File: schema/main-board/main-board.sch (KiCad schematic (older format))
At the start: 75 parts, among them P1 TST, P10 TST, P11 CONN_20, P12 CONN_4, P13 CONN_4, P14 CONN_4, P2 TST, P3 TST, P4 TST, P5 TST, P6 TST, P7 TST, P8 TST, P9 TST, Q1 bc847, Q2 si2301, Q3 si2301, Q4 irll2703, Q5 bc847, Q6 bc857, Q7 si2301, Q8 si2301, U1 L293, U2 NCP3063, U3 NCP3063

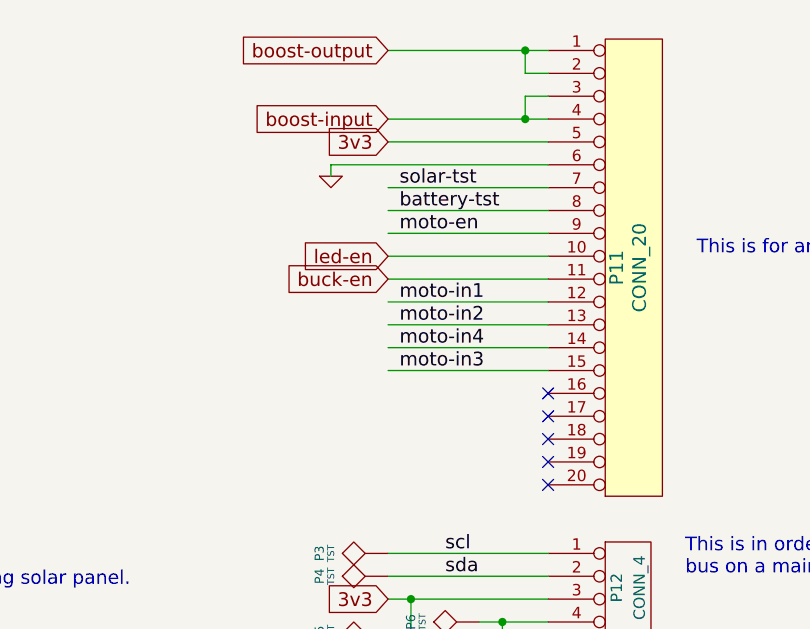
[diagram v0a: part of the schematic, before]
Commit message: Rearranged pins to match control-board's socket pinout.
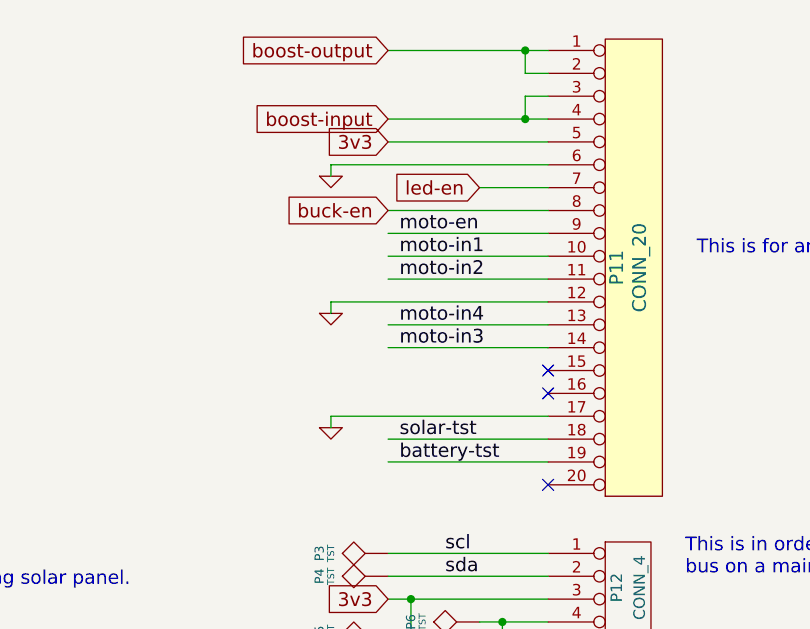
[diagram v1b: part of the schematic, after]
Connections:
- wire segments 231 -> 235
- no-connect marks 5 -> 3
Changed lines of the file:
@@
-EESchema Schematic File Version 2  date Thu 30 Aug 2012 02:28:51 PM MSK
+EESchema Schematic File Version 2  date Thu 30 Aug 2012 03:00:08 PM MSK
 LIBS:power
 LIBS:device
@@
 Comment4 ""
 $EndDescr
+NoConn ~ 4800 7450
+Wire Wire Line
+	3850 7600 3850 7550
+Wire Wire Line
+	3850 7550 4800 7550
+Wire Wire Line
+	4800 6650 4100 6650
 Connection ~ 7100 2250
 Wire Wire Line
@@
 	4800 6350 4100 6350
 Wire Wire Line
-	4800 7350 4100 7350
-Wire Wire Line
-	4800 7150 4100 7150
+	4800 7250 4100 7250
 Wire Wire Line
 	4800 6950 4100 6950
@@
 	4800 6750 4100 6750
 Wire Wire Line
-	4800 6550 4100 6550
+	4800 7650 4100 7650
 Wire Wire Line
 	7700 10300 7300 10300
@@
 Connection ~ 8950 8300
 Wire Wire Line
-	4800 6650 4100 6650
+	4800 7750 4100 7750
 Wire Wire Line
 	4800 6850 4100 6850
 Wire Wire Line
-	4800 7050 4100 7050
-Wire Wire Line
-	4800 7250 4100 7250
+	4800 7150 4100 7150
 Wire Wire Line
 	4800 6450 3850 6450
@@
 Wire Wire Line
 	6700 750  6700 2450
+Wire Wire Line
+	4800 6550 4500 6550
+Wire Wire Line
+	4800 7050 3850 7050
+Wire Wire Line
+	3850 7050 3850 7100
+$Comp
+L GND #PWR?
+U 1 1 503F475C
+P 3850 7600
+F 0 "#PWR?" H 3850 7600 30  0001 C CNN
+F 1 "GND" H 3850 7530 30  0001 C CNN
+	1    3850 7600
+	1    0    0    -1
+$EndComp
+$Comp
+L GND #PWR?
+U 1 1 503F472D
+P 3850 7100
+F 0 "#PWR?" H 3850 7100 30  0001 C CNN
+F 1 "GND" H 3850 7030 30  0001 C CNN
+	1    3850 7100
+	1    0    0    -1
+$EndComp
 $Comp
 L PWR_FLAG #FLG01
@@
 $EndComp
 NoConn ~ 4800 7850
-NoConn ~ 4800 7750
-NoConn ~ 4800 7650
-NoConn ~ 4800 7550
-NoConn ~ 4800 7450
+NoConn ~ 4800 7350
 $Comp
 L GND #PWR023
@@
 	1    0    0    -1
 $EndComp
+Text Label 4150 7150 0    60   ~ 0
+moto-in4
 Text Label 4150 7250 0    60   ~ 0
-moto-in4
-Text Label 4150 7350 0    60   ~ 0
 moto-in3
-Text Label 4150 7150 0    60   ~ 0
+Text Label 4150 6950 0    60   ~ 0
 moto-in2
-Text Label 4150 7050 0    60   ~ 0
+Text Label 4150 6850 0    60   ~ 0
 moto-in1
-Text GLabel 4100 6950 0    60   Input ~ 0
+Text GLabel 4100 6650 0    60   Input ~ 0
 buck-en
-Text GLabel 4100 6850 0    60   Input ~ 0
+Text GLabel 4500 6550 0    60   Input ~ 0
 led-en
 Text Label 4150 6750 0    60   ~ 0
 moto-en
-Text Label 4150 6650 0    60   ~ 0
+Text Label 4150 7750 0    60   ~ 0
 battery-tst
-Text Label 4150 6550 0    60   ~ 0
+Text Label 4150 7650 0    60   ~ 0
 solar-tst
 Text GLabel 8650 8300 0    60   Input ~ 0
